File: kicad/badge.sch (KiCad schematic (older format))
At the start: 8 parts

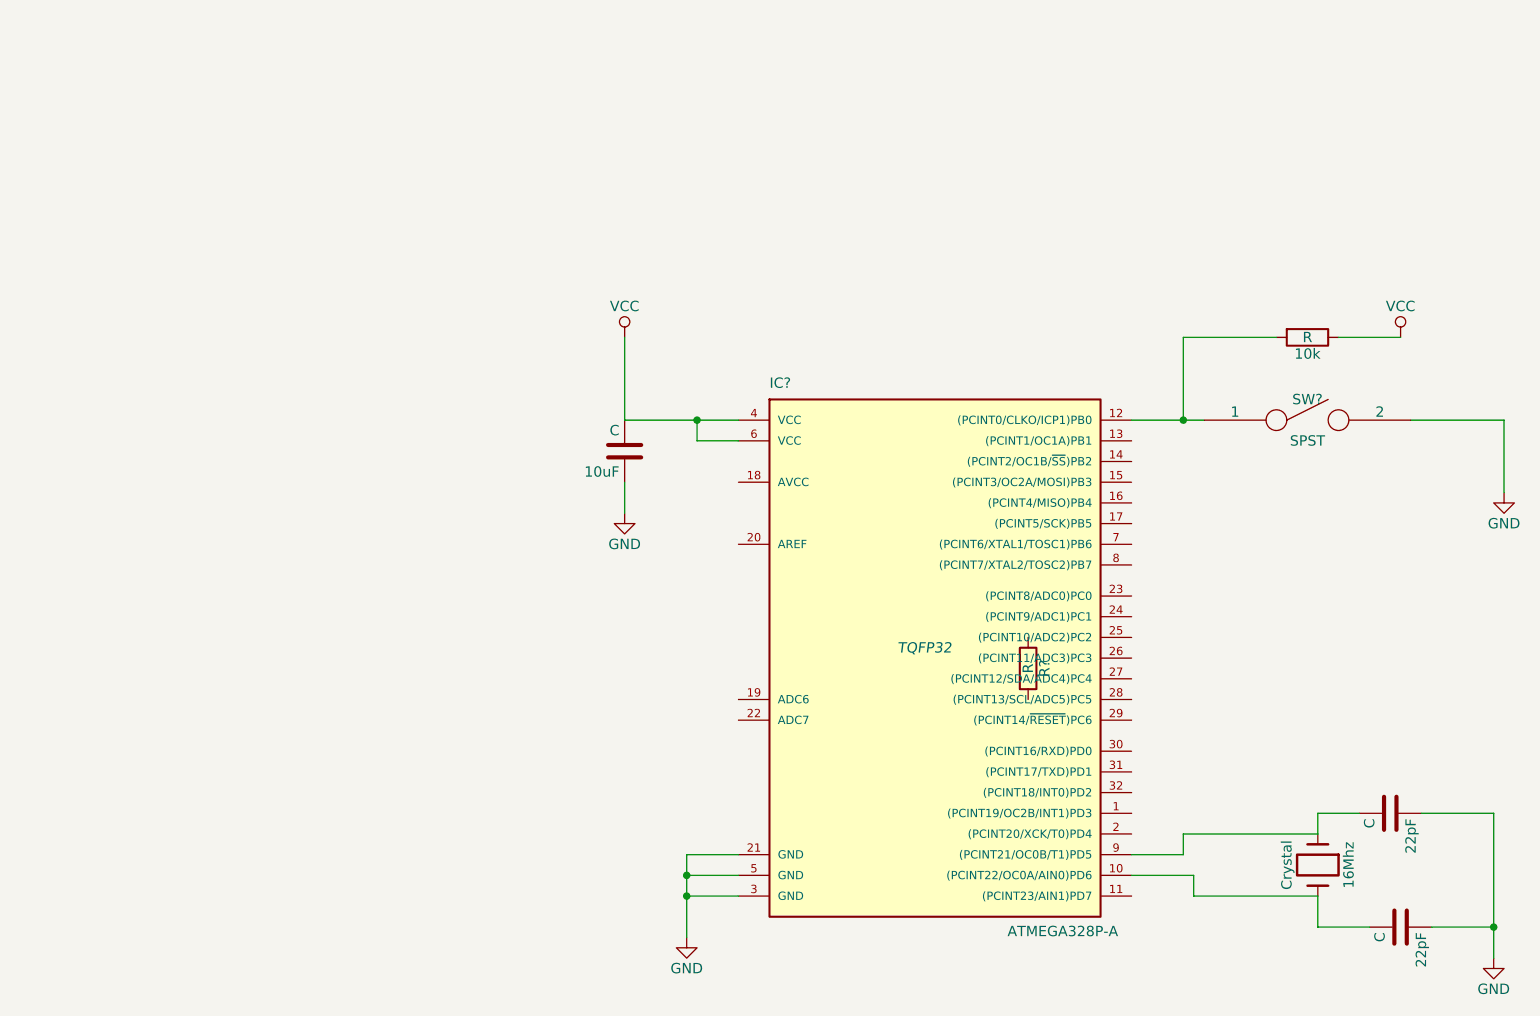
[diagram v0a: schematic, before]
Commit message: voltage regulator
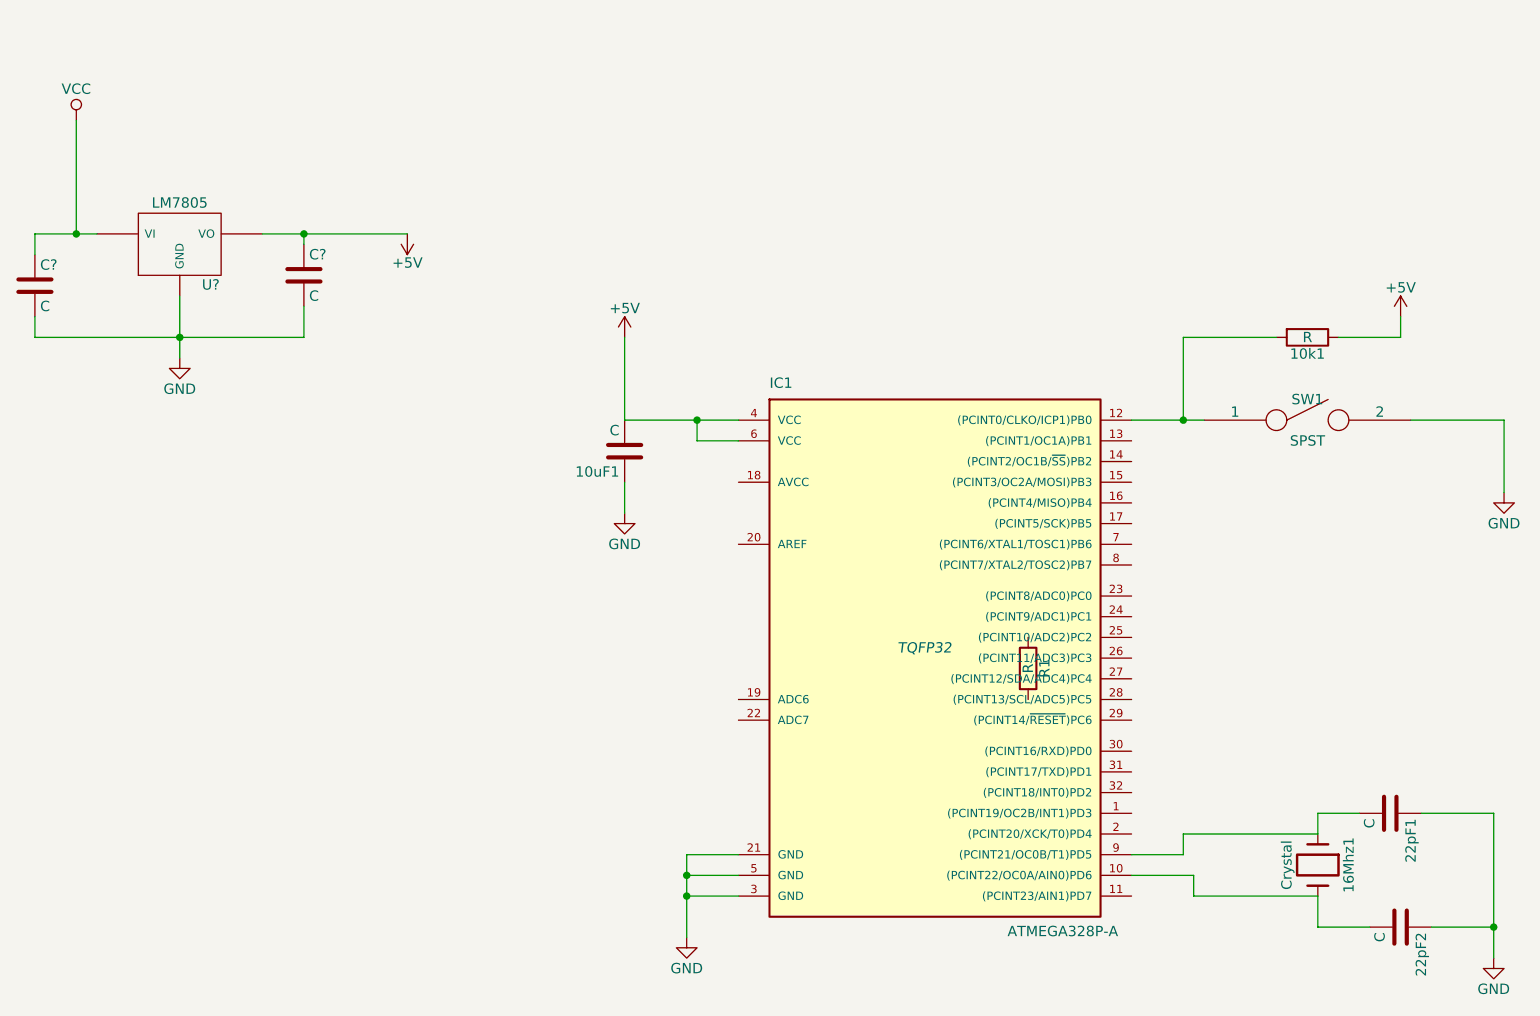
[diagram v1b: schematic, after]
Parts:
- added C? (x2): C, symbol C
- added U?: LM7805, symbol LM7805
- gave numbers to parts that had none: 3
- renumbered 10k to 10k1, 10uF to 10uF1, 16Mhz to 16Mhz1, 22pF to 22pF1, 22pF to 22pF2
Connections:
- net GND: now also C?.2, C?.2, U?.GND
- net VCC: now also C?.1, U?.VI; no longer 10k1.1, 10uF1.2, IC1.4 (VCC), IC1.6 (VCC)
- new net +5V: 10k1.1, 10uF1.2, C?.1, IC1.4 (VCC), IC1.6 (VCC), U?.VO
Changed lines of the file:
@@
 LIBS:contrib
 LIBS:valves
+LIBS:badge-cache
 EELAYER 25 0
 EELAYER END
@@
 $EndDescr
 $Comp
-L R R?
+L R R1
 U 1 1 58E158FB
 P 6100 3850
-F 0 "R?" V 6180 3850 50  0000 C CNN
+F 0 "R1" V 6180 3850 50  0000 C CNN
 F 1 "R" V 6100 3850 50  0000 C CNN
 F 2 "" V 6030 3850 50  0000 C CNN
@@
 $EndComp
 $Comp
-L ATMEGA328P-A IC?
+L ATMEGA328P-A IC1
 U 1 1 58E15973
 P 5600 3750
-F 0 "IC?" H 4850 5000 50  0000 L BNN
+F 0 "IC1" H 4850 5000 50  0000 L BNN
 F 1 "ATMEGA328P-A" H 6000 2350 50  0000 L BNN
 F 2 "TQFP32" H 5600 3750 50  0000 C CIN
@@
 $EndComp
 $Comp
-L GND #PWR?
+L GND #PWR01
 U 1 1 58E15A16
 P 4450 5150
-F 0 "#PWR?" H 4450 4900 50  0001 C CNN
+F 0 "#PWR01" H 4450 4900 50  0001 C CNN
 F 1 "GND" H 4450 5000 50  0000 C CNN
 F 2 "" H 4450 5150 50  0000 C CNN
@@
 $EndComp
 $Comp
-L VCC #PWR?
-U 1 1 58E15A4F
-P 4150 2250
-F 0 "#PWR?" H 4150 2100 50  0001 C CNN
-F 1 "VCC" H 4150 2400 50  0000 C CNN
-F 2 "" H 4150 2250 50  0000 C CNN
-F 3 "" H 4150 2250 50  0000 C CNN
-	1    4150 2250
-	1    0    0    -1
-$EndComp
-$Comp
-L VCC #PWR?
-U 1 1 58E15AA9
-P 7900 2250
-F 0 "#PWR?" H 7900 2100 50  0001 C CNN
-F 1 "VCC" H 7900 2400 50  0000 C CNN
-F 2 "" H 7900 2250 50  0000 C CNN
-F 3 "" H 7900 2250 50  0000 C CNN
-	1    7900 2250
-	1    0    0    -1
-$EndComp
-$Comp
-L R 10k
+L R 10k1
 U 1 1 58E15AC1
 P 7450 2250
-F 0 "10k" V 7530 2250 50  0000 C CNN
+F 0 "10k1" V 7530 2250 50  0000 C CNN
 F 1 "R" V 7450 2250 50  0000 C CNN
 F 2 "" V 7380 2250 50  0000 C CNN
@@
 $EndComp
 $Comp
-L Crystal 16Mhz
+L Crystal 16Mhz1
 U 1 1 58E15B48
 P 7500 4800
-F 0 "16Mhz" H 7500 4950 50  0000 C CNN
+F 0 "16Mhz1" H 7500 4950 50  0000 C CNN
 F 1 "Crystal" H 7500 4650 50  0000 C CNN
 F 2 "" H 7500 4800 50  0000 C CNN
@@
 $EndComp
 $Comp
-L C 22pF
+L C 22pF1
 U 1 1 58E15B8A
 P 7850 4550
-F 0 "22pF" H 7875 4650 50  0000 L CNN
+F 0 "22pF1" H 7875 4650 50  0000 L CNN
 F 1 "C" H 7875 4450 50  0000 L CNN
 F 2 "" H 7888 4400 50  0000 C CNN
@@
 $EndComp
 $Comp
-L C 22pF
+L C 22pF2
 U 1 1 58E15BB3
 P 7900 5100
-F 0 "22pF" H 7925 5200 50  0000 L CNN
+F 0 "22pF2" H 7925 5200 50  0000 L CNN
 F 1 "C" H 7925 5000 50  0000 L CNN
 F 2 "" H 7938 4950 50  0000 C CNN
@@
 	0    1    1    0
 $EndComp
-Wire Wire Line
-	6600 4850 6900 4850
-Wire Wire Line
-	6900 4850 6900 4950
-Wire Wire Line
-	6600 4750 6850 4750
-Wire Wire Line
-	6850 4750 6850 4650
-Wire Wire Line
-	6850 4650 7500 4650
-Wire Wire Line
-	7500 4550 7700 4550
-Wire Wire Line
-	7500 4650 7500 4550
-Wire Wire Line
-	6900 4950 7500 4950
-Wire Wire Line
-	7500 4950 7500 5100
-Wire Wire Line
-	7500 5100 7750 5100
-$Comp
-L GND #PWR?
+$Comp
+L GND #PWR04
 U 1 1 58E16135
 P 8350 5250
-F 0 "#PWR?" H 8350 5000 50  0001 C CNN
+F 0 "#PWR04" H 8350 5000 50  0001 C CNN
 F 1 "GND" H 8350 5100 50  0000 C CNN
 F 2 "" H 8350 5250 50  0000 C CNN
@@
 	1    0    0    -1
 $EndComp
-Wire Wire Line
-	8000 4550 8350 4550
-Wire Wire Line
-	8350 4550 8350 5100
-Wire Wire Line
-	8350 5100 8350 5250
-Wire Wire Line
-	8050 5100 8350 5100
-Connection ~ 8350 5100
-Wire Wire Line
-	4700 4750 4450 4750
-Wire Wire Line
-	4450 4750 4450 4850
-Wire Wire Line
-	4450 4850 4450 4950
-Wire Wire Line
-	4450 4950 4450 5150
-Wire Wire Line
-	4700 4950 4450 4950
-Connection ~ 4450 4950
-Wire Wire Line
-	4700 4850 4450 4850
-Connection ~ 4450 4850
-Wire Wire Line
-	4150 2650 4500 2650
-Wire Wire Line
-	4500 2650 4700 2650
-Wire Wire Line
-	4150 2650 4150 2250
-Wire Wire Line
-	4700 2750 4500 2750
-Wire Wire Line
-	4500 2750 4500 2650
-Connection ~ 4500 2650
-$Comp
-L C 10uF
+$Comp
+L C 10uF1
 U 1 1 58E164D8
 P 4150 2800
-F 0 "10uF" H 4175 2900 50  0000 L CNN
+F 0 "10uF1" H 4175 2900 50  0000 L CNN
 F 1 "C" H 4175 2700 50  0000 L CNN
 F 2 "" H 4188 2650 50  0000 C CNN
@@
 $EndComp
 $Comp
-L GND #PWR?
+L GND #PWR05
 U 1 1 58E16557
 P 4150 3100
-F 0 "#PWR?" H 4150 2850 50  0001 C CNN
+F 0 "#PWR05" H 4150 2850 50  0001 C CNN
 F 1 "GND" H 4150 2950 50  0000 C CNN
 F 2 "" H 4150 3100 50  0000 C CNN
@@
 	1    0    0    -1
 $EndComp
-Wire Wire Line
-	4150 2950 4150 3100
-$Comp
-L SPST SW?
+$Comp
+L SPST SW1
 U 1 1 58E1666E
 P 7450 2650
-F 0 "SW?" H 7450 2750 50  0000 C CNN
+F 0 "SW1" H 7450 2750 50  0000 C CNN
 F 1 "SPST" H 7450 2550 50  0000 C CNN
 F 2 "" H 7450 2650 50  0000 C CNN
@@
 $EndComp
 $Comp
-L GND #PWR?
+L GND #PWR06
 U 1 1 58E166C3
 P 8400 3000
-F 0 "#PWR?" H 8400 2750 50  0001 C CNN
+F 0 "#PWR06" H 8400 2750 50  0001 C CNN
 F 1 "GND" H 8400 2850 50  0000 C CNN
 F 2 "" H 8400 3000 50  0000 C CNN
@@
 	1    0    0    -1
 $EndComp
+$Comp
+L LM7805 U?
+U 1 1 58E194B3
+P 2000 1800
+F 0 "U?" H 2150 1604 50  0000 C CNN
+F 1 "LM7805" H 2000 2000 50  0000 C CNN
+F 2 "" H 2000 1800 50  0000 C CNN
+F 3 "" H 2000 1800 50  0000 C CNN
+	1    2000 1800
+	1    0    0    -1
+$EndComp
+$Comp
+L GND #PWR?
+U 1 1 58E194EE
+P 2000 2350
+F 0 "#PWR?" H 2000 2100 50  0001 C CNN
+F 1 "GND" H 2000 2200 50  0000 C CNN
+F 2 "" H 2000 2350 50  0000 C CNN
+F 3 "" H 2000 2350 50  0000 C CNN
+	1    2000 2350
+	1    0    0    -1
+$EndComp
+$Comp
+L C C?
+U 1 1 58E19514
+P 2600 1950
+F 0 "C?" H 2625 2050 50  0000 L CNN
+F 1 "C" H 2625 1850 50  0000 L CNN
+F 2 "" H 2638 1800 50  0000 C CNN
+F 3 "" H 2600 1950 50  0000 C CNN
+	1    2600 1950
+	1    0    0    -1
+$EndComp
+$Comp
+L C C?
+U 1 1 58E19563
+P 1300 2000
+F 0 "C?" H 1325 2100 50  0000 L CNN
+F 1 "C" H 1325 1900 50  0000 L CNN
+F 2 "" H 1338 1850 50  0000 C CNN
+F 3 "" H 1300 2000 50  0000 C CNN
+	1    1300 2000
+	1    0    0    -1
+$EndComp
+$Comp
+L +5V #PWR?
+U 1 1 58E1975A
+P 3100 1750
+F 0 "#PWR?" H 3100 1600 50  0001 C CNN
+F 1 "+5V" H 3100 1890 50  0000 C CNN
+F 2 "" H 3100 1750 50  0000 C CNN
+F 3 "" H 3100 1750 50  0000 C CNN
+	1    3100 1750
+	-1   0    0    1
+$EndComp
+$Comp
+L +5V #PWR?
+U 1 1 58E1983D
+P 4150 2250
+F 0 "#PWR?" H 4150 2100 50  0001 C CNN
+F 1 "+5V" H 4150 2390 50  0000 C CNN
+F 2 "" H 4150 2250 50  0000 C CNN
+F 3 "" H 4150 2250 50  0000 C CNN
+	1    4150 2250
+	1    0    0    -1
+$EndComp
+$Comp
+L +5V #PWR?
+U 1 1 58E198B5
+P 7900 2150
+F 0 "#PWR?" H 7900 2000 50  0001 C CNN
+F 1 "+5V" H 7900 2290 50  0000 C CNN
+F 2 "" H 7900 2150 50  0000 C CNN
+F 3 "" H 7900 2150 50  0000 C CNN
+	1    7900 2150
+	1    0    0    -1
+$EndComp
+Wire Wire Line
+	6600 4850 6900 4850
+Wire Wire Line
+	6900 4850 6900 4950
+Wire Wire Line
+	6600 4750 6850 4750
+Wire Wire Line
+	6850 4750 6850 4650
+Wire Wire Line
+	6850 4650 7500 4650
+Wire Wire Line
+	7500 4550 7700 4550
+Wire Wire Line
+	7500 4650 7500 4550
+Wire Wire Line
+	6900 4950 7500 4950
+Wire Wire Line
+	7500 4950 7500 5100
+Wire Wire Line
+	7500 5100 7750 5100
+Wire Wire Line
+	8000 4550 8350 4550
+Wire Wire Line
+	8350 4550 8350 5250
+Wire Wire Line
+	8050 5100 8350 5100
+Connection ~ 8350 5100
+Wire Wire Line
+	4700 4750 4450 4750
+Wire Wire Line
+	4450 4750 4450 5150
+Wire Wire Line
+	4700 4950 4450 4950
+Connection ~ 4450 4950
+Wire Wire Line
+	4700 4850 4450 4850
+Connection ~ 4450 4850
+Wire Wire Line
+	4150 2650 4700 2650
+Wire Wire Line
+	4150 2650 4150 2250
+Wire Wire Line
+	4700 2750 4500 2750
+Wire Wire Line
+	4500 2750 4500 2650
+Connection ~ 4500 2650
+Wire Wire Line
+	4150 2950 4150 3100
 Wire Wire Line
 	7950 2650 8400 2650
@@
 	8400 2650 8400 3000
 Wire Wire Line
-	6950 2650 6850 2650
-Wire Wire Line
-	6850 2650 6600 2650
+	6600 2650 6950 2650
 Wire Wire Line
 	7300 2250 6850 2250
@@
 Wire Wire Line
 	7900 2250 7600 2250
+Wire Wire Line
+	1600 1750 1300 1750
+Wire Wire Line
+	1300 1750 1300 1850
+Wire Wire Line
+	2000 2050 2000 2350
+Wire Wire Line
+	1300 2150 1300 2250
+Wire Wire Line
+	1300 2250 2600 2250
+Connection ~ 2000 2250
+Wire Wire Line
+	2600 2250 2600 2100
+Wire Wire Line
+	2400 1750 3100 1750
+Wire Wire Line
+	2600 1750 2600 1800
+Connection ~ 2600 1750
+Wire Wire Line
+	7900 2150 7900 2250
+$Comp
+L VCC #PWR?
+U 1 1 58E19A0A
+P 1500 1200
+F 0 "#PWR?" H 1500 1050 50  0001 C CNN
+F 1 "VCC" H 1500 1350 50  0000 C CNN
+F 2 "" H 1500 1200 50  0000 C CNN
+F 3 "" H 1500 1200 50  0000 C CNN
+	1    1500 1200
+	1    0    0    -1
+$EndComp
+Wire Wire Line
+	1500 1200 1500 1750
+Connection ~ 1500 1750
 $EndSCHEMATC

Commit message: replace: A4MEGA328-A -> A4MEGA328-P
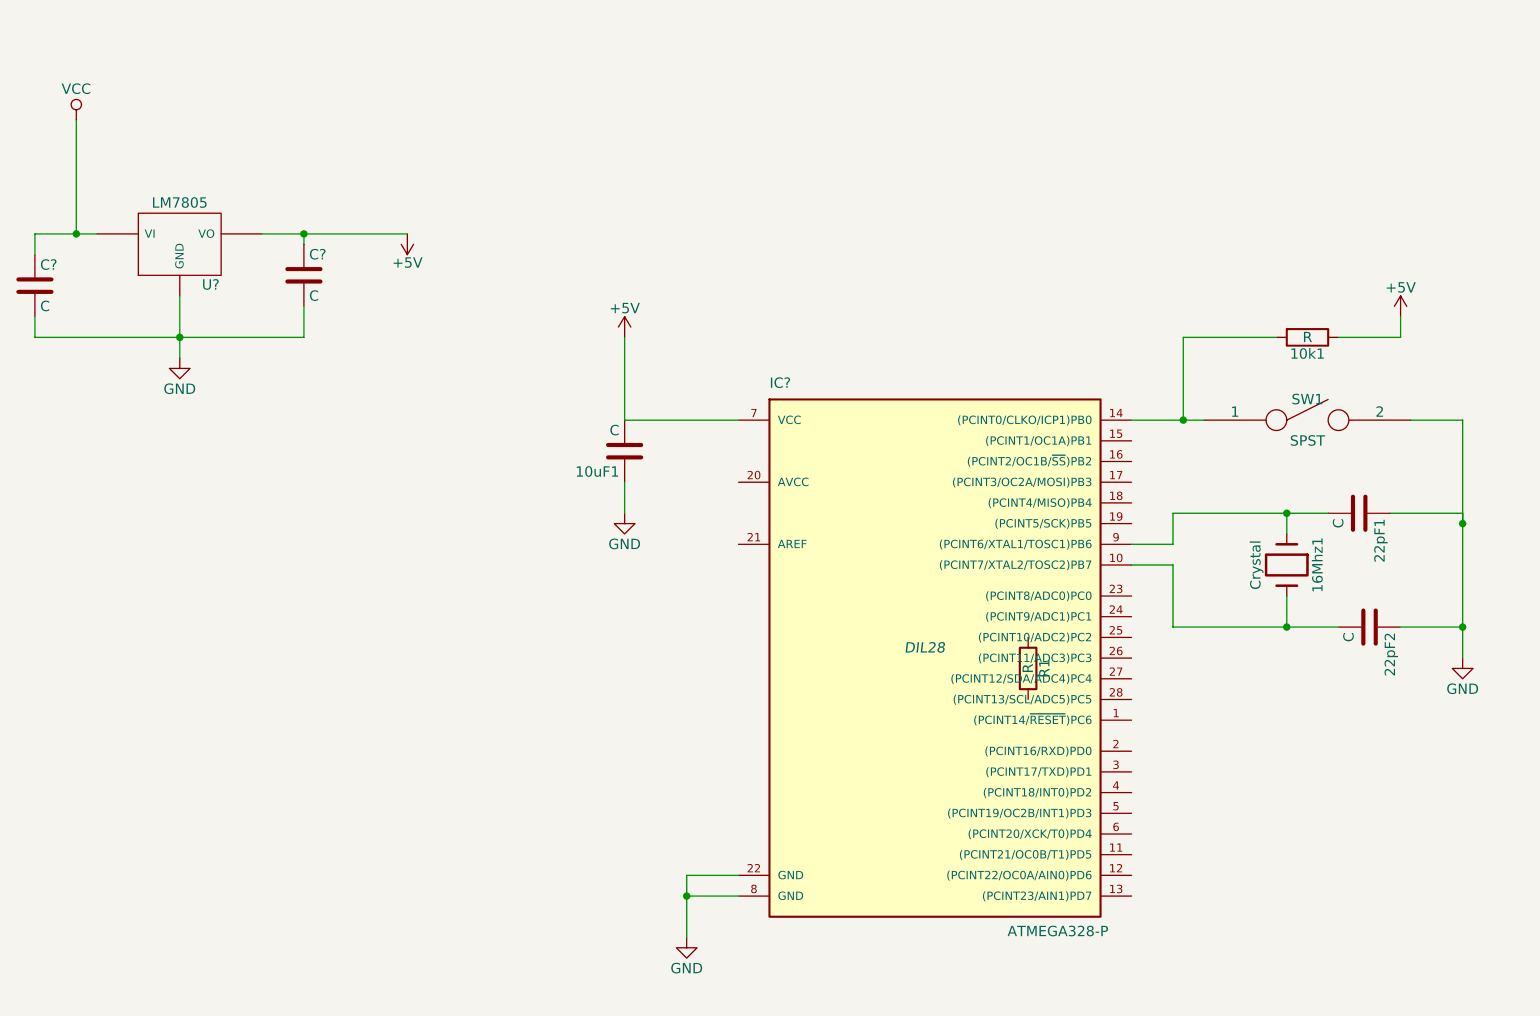
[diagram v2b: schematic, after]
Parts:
- removed IC1: ATMEGA328P-A, TQFP32, symbol ATMEGA328P-A
- added IC?: ATMEGA328-P, DIL28, symbol ATMEGA328-P
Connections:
- net +5V: now also IC?.7 (VCC)
- net GND: now also IC?.22 (GND), IC?.8 (GND)
- net at 16Mhz1.2, 22pF2.2: now also IC?.10 ((PCINT7/XTAL2/TOSC2)PB7)
- net at 10k1.2, SW1.1: now also IC?.14 ((PCINT0/CLKO/ICP1)PB0)
- net at 16Mhz1.1, 22pF1.2: now also IC?.9 ((PCINT6/XTAL1/TOSC1)PB6)
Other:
- moved on the sheet: 16Mhz1, 22pF1, 22pF2
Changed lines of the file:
@@
-$EndComp
-$Comp
-L ATMEGA328P-A IC1
-U 1 1 58E15973
-P 5600 3750
-F 0 "IC1" H 4850 5000 50  0000 L BNN
-F 1 "ATMEGA328P-A" H 6000 2350 50  0000 L BNN
-F 2 "TQFP32" H 5600 3750 50  0000 C CIN
-F 3 "" H 5600 3750 50  0000 C CNN
-	1    5600 3750
-	1    0    0    -1
 $EndComp
 $Comp
@@
 L Crystal 16Mhz1
 U 1 1 58E15B48
-P 7500 4800
-F 0 "16Mhz1" H 7500 4950 50  0000 C CNN
-F 1 "Crystal" H 7500 4650 50  0000 C CNN
-F 2 "" H 7500 4800 50  0000 C CNN
-F 3 "" H 7500 4800 50  0000 C CNN
-	1    7500 4800
+P 7350 3350
+F 0 "16Mhz1" H 7350 3500 50  0000 C CNN
+F 1 "Crystal" H 7350 3200 50  0000 C CNN
+F 2 "" H 7350 3350 50  0000 C CNN
+F 3 "" H 7350 3350 50  0000 C CNN
+	1    7350 3350
 	0    1    1    0
 $EndComp
@@
 L C 22pF1
 U 1 1 58E15B8A
-P 7850 4550
-F 0 "22pF1" H 7875 4650 50  0000 L CNN
-F 1 "C" H 7875 4450 50  0000 L CNN
-F 2 "" H 7888 4400 50  0000 C CNN
-F 3 "" H 7850 4550 50  0000 C CNN
-	1    7850 4550
+P 7700 3100
+F 0 "22pF1" H 7725 3200 50  0000 L CNN
+F 1 "C" H 7725 3000 50  0000 L CNN
+F 2 "" H 7738 2950 50  0000 C CNN
+F 3 "" H 7700 3100 50  0000 C CNN
+	1    7700 3100
 	0    1    1    0
 $EndComp
@@
 L C 22pF2
 U 1 1 58E15BB3
-P 7900 5100
-F 0 "22pF2" H 7925 5200 50  0000 L CNN
-F 1 "C" H 7925 5000 50  0000 L CNN
-F 2 "" H 7938 4950 50  0000 C CNN
-F 3 "" H 7900 5100 50  0000 C CNN
-	1    7900 5100
+P 7750 3650
+F 0 "22pF2" H 7775 3750 50  0000 L CNN
+F 1 "C" H 7775 3550 50  0000 L CNN
+F 2 "" H 7788 3500 50  0000 C CNN
+F 3 "" H 7750 3650 50  0000 C CNN
+	1    7750 3650
 	0    1    1    0
 $EndComp
@@
 L GND #PWR04
 U 1 1 58E16135
-P 8350 5250
-F 0 "#PWR04" H 8350 5000 50  0001 C CNN
-F 1 "GND" H 8350 5100 50  0000 C CNN
-F 2 "" H 8350 5250 50  0000 C CNN
-F 3 "" H 8350 5250 50  0000 C CNN
-	1    8350 5250
+P 8200 3800
+F 0 "#PWR04" H 8200 3550 50  0001 C CNN
+F 1 "GND" H 8200 3650 50  0000 C CNN
+F 2 "" H 8200 3800 50  0000 C CNN
+F 3 "" H 8200 3800 50  0000 C CNN
+	1    8200 3800
 	1    0    0    -1
 $EndComp
@@
 $EndComp
 $Comp
-L GND #PWR06
-U 1 1 58E166C3
-P 8400 3000
-F 0 "#PWR06" H 8400 2750 50  0001 C CNN
-F 1 "GND" H 8400 2850 50  0000 C CNN
-F 2 "" H 8400 3000 50  0000 C CNN
-F 3 "" H 8400 3000 50  0000 C CNN
-	1    8400 3000
-	1    0    0    -1
-$EndComp
-$Comp
 L LM7805 U?
 U 1 1 58E194B3
@@
 $EndComp
 Wire Wire Line
-	6600 4850 6900 4850
-Wire Wire Line
-	6900 4850 6900 4950
-Wire Wire Line
-	6600 4750 6850 4750
-Wire Wire Line
-	6850 4750 6850 4650
-Wire Wire Line
-	6850 4650 7500 4650
-Wire Wire Line
-	7500 4550 7700 4550
-Wire Wire Line
-	7500 4650 7500 4550
-Wire Wire Line
-	6900 4950 7500 4950
-Wire Wire Line
-	7500 4950 7500 5100
-Wire Wire Line
-	7500 5100 7750 5100
-Wire Wire Line
-	8000 4550 8350 4550
-Wire Wire Line
-	8350 4550 8350 5250
-Wire Wire Line
-	8050 5100 8350 5100
-Connection ~ 8350 5100
-Wire Wire Line
-	4700 4750 4450 4750
-Wire Wire Line
-	4450 4750 4450 5150
+	6800 3100 7550 3100
+Wire Wire Line
+	7350 3200 7350 3100
+Wire Wire Line
+	7350 3500 7350 3650
+Wire Wire Line
+	6800 3650 7600 3650
+Wire Wire Line
+	7850 3100 8200 3100
+Wire Wire Line
+	8200 3100 8200 3800
+Wire Wire Line
+	7900 3650 8200 3650
+Connection ~ 8200 3650
 Wire Wire Line
 	4700 4950 4450 4950
@@
 Wire Wire Line
 	4700 4850 4450 4850
-Connection ~ 4450 4850
 Wire Wire Line
 	4150 2650 4700 2650
@@
 	4150 2650 4150 2250
 Wire Wire Line
-	4700 2750 4500 2750
-Wire Wire Line
-	4500 2750 4500 2650
-Connection ~ 4500 2650
-Wire Wire Line
 	4150 2950 4150 3100
-Wire Wire Line
-	7950 2650 8400 2650
-Wire Wire Line
-	8400 2650 8400 3000
 Wire Wire Line
 	6600 2650 6950 2650
@@
 	7900 2250 7600 2250
 Wire Wire Line
-	1600 1750 1300 1750
+	1300 1750 1600 1750
 Wire Wire Line
 	1300 1750 1300 1850
@@
 	1500 1200 1500 1750
 Connection ~ 1500 1750
+$Comp
+L ATMEGA328-P IC?
+U 1 1 58E19C48
+P 5600 3750
+F 0 "IC?" H 4850 5000 50  0000 L BNN
+F 1 "ATMEGA328-P" H 6000 2350 50  0000 L BNN
+F 2 "DIL28" H 5600 3750 50  0000 C CIN
+F 3 "" H 5600 3750 50  0000 C CNN
+	1    5600 3750
+	1    0    0    -1
+$EndComp
+Wire Wire Line
+	6600 3250 6800 3250
+Wire Wire Line
+	6800 3250 6800 3100
+Connection ~ 7350 3100
+Wire Wire Line
+	6600 3350 6800 3350
+Wire Wire Line
+	6800 3350 6800 3650
+Connection ~ 7350 3650
+Wire Wire Line
+	4450 4850 4450 5150
+Wire Wire Line
+	7950 2650 8200 2650
+Wire Wire Line
+	8200 2650 8200 3150
+Connection ~ 8200 3150
 $EndSCHEMATC
